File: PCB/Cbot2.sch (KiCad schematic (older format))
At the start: 26 parts, among them J1 +5V Power, J10 Pads, J11 Pads, J12 Pads, J2 +5V RPi Power, J3 Raspberry_Pi_2_3, J4 Lights, J5 Fan, J6 Switch, J7 Amplifier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

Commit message: PCB update
Move signal from Raspberry Pi pin 12 to pin 11.
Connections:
- net FAN: now reaches J3.11 (GPIO17)
- net FAN: now also R1.2
- net PWM0: no longer names the net of J3.12 (GPIO18/PWM0)
- net PWM0: no longer R1.2
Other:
- note added: "January 26, 2020"
- note removed: "1.0"
- note removed: "CordieBot: Connection HAT"
- note removed: "December 19, 2019"
- moved on the sheet: C1, C2, C3, D1, H1, H2, H3, H4, J1, J2, J3, J4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

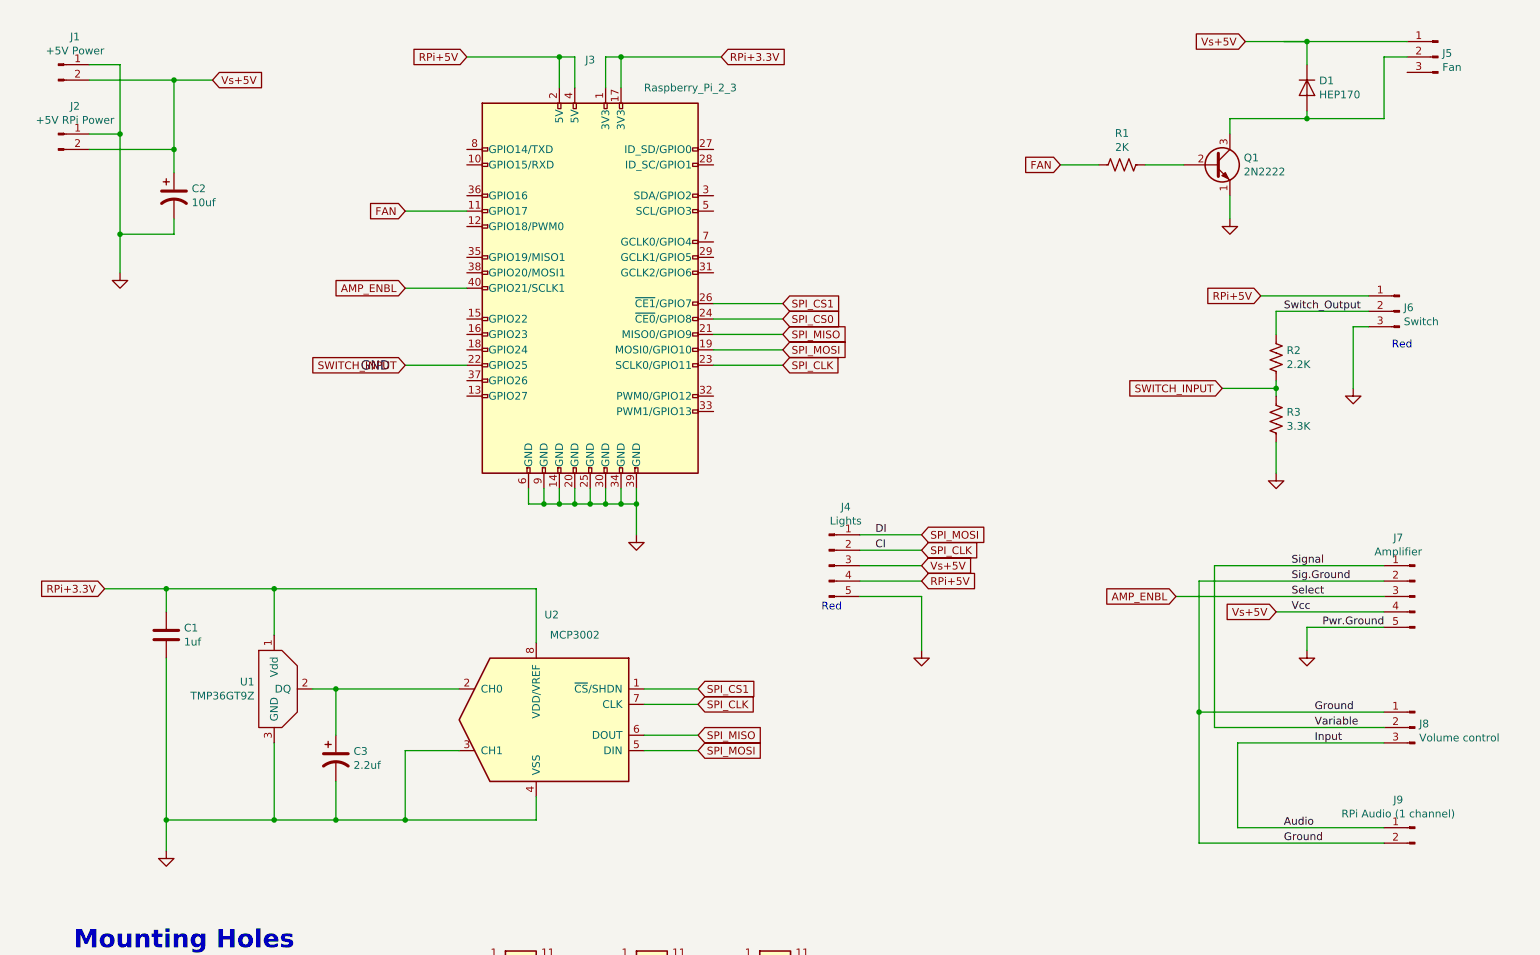
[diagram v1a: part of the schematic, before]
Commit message: PCB Updates
Annotate connectors and RED markings.
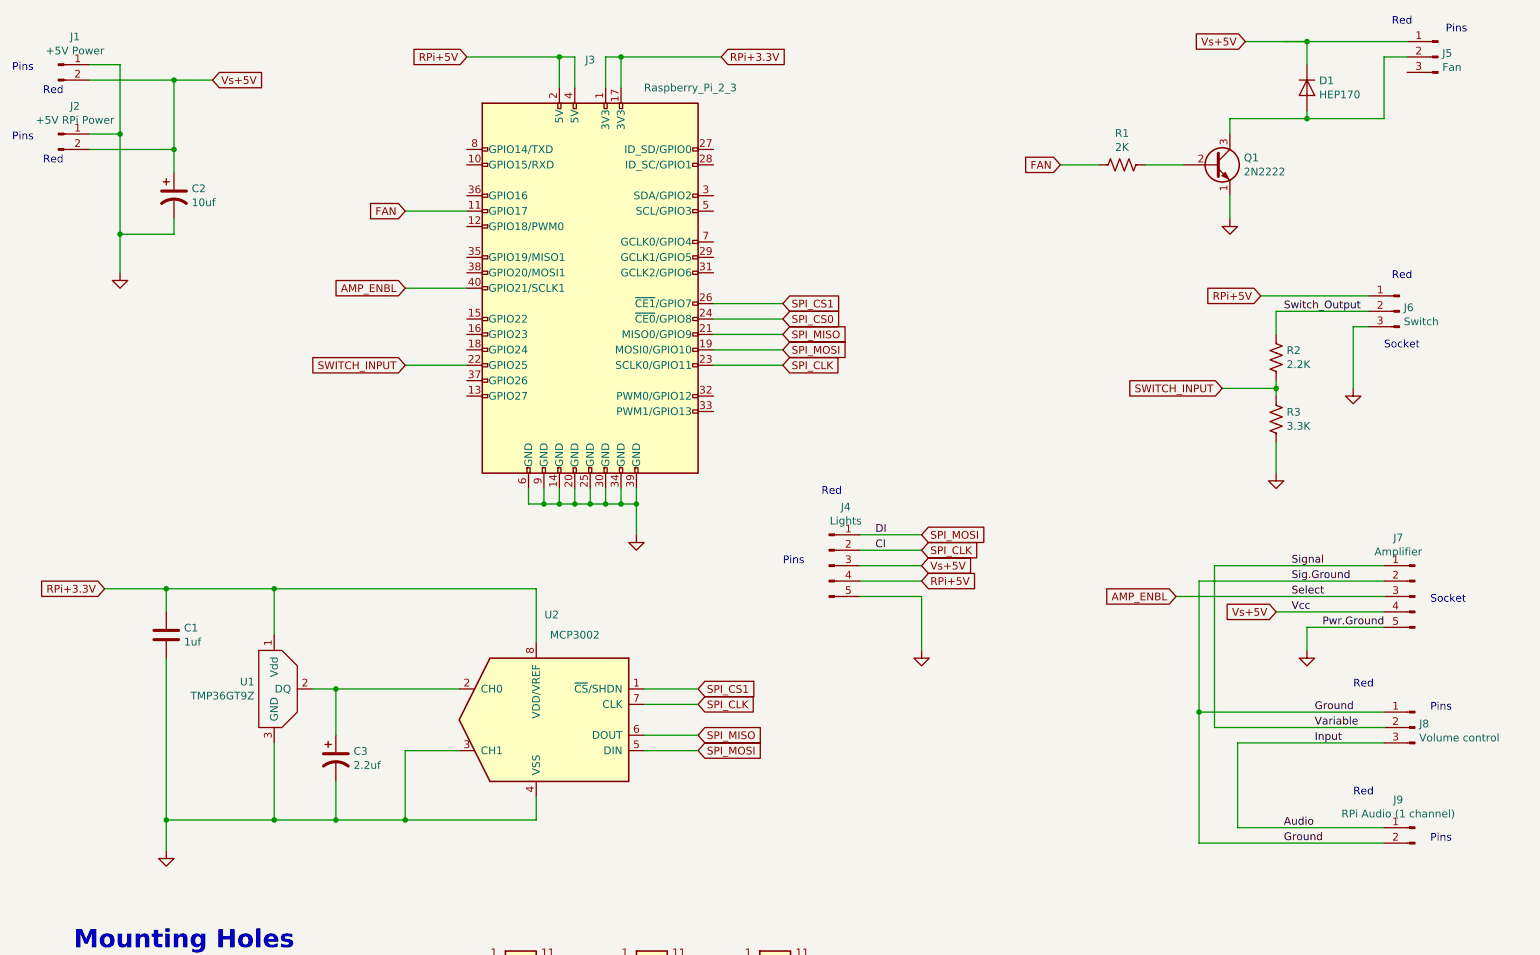
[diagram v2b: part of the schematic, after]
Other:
- note added: "Pins"
- note added: "Socket"
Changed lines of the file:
@@
 	1    0    0    -1
 $EndComp
-Text Notes 9700 2900 0    50   ~ 0
-Red
-Text Notes 6000 4600 0    50   ~ 0
+Text Notes 9700 2450 0    50   ~ 0
+Red
+Text Notes 6000 3850 0    50   ~ 0
 Red
 Text Label 6350 4100 0    50   ~ 0
@@
 Text Notes 1150 6800 0    118  ~ 24
 Mounting Holes
-Text Label 3200 3050 2    60   ~ 0
-GND
 $Comp
 L Connector_Generic:Conn_02x10_Top_Bottom J10
@@
 Text Notes 7450 7850 0    50   ~ 0
 January 26, 2020
+Text Notes 9700 800  0    50   ~ 0
+Red
+Text Notes 9450 5800 0    50   ~ 0
+Red
+Text Notes 9450 5100 0    50   ~ 0
+Red
+Text Notes 950  1250 0    50   ~ 0
+Red
+Text Notes 950  1700 0    50   ~ 0
+Red
+Text Notes 9950 6100 0    50   ~ 0
+Pins
+Text Notes 9950 5250 0    50   ~ 0
+Pins
+Text Notes 10050 850  0    50   ~ 0
+Pins
+Text Notes 5750 4300 0    50   ~ 0
+Pins
+Text Notes 750  1100 0    50   ~ 0
+Pins
+Text Notes 750  1550 0    50   ~ 0
+Pins
+Text Notes 9650 2900 0    50   ~ 0
+Socket
+Text Notes 9950 4550 0    50   ~ 0
+Socket
 $EndSCHEMATC
